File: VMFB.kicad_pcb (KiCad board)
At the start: 2 copper layers, 141.6 x 109.9 mm, 109 parts, among them J1 Barrel_Jack_Switch, J10 Conn_01x03_Pin, J11 Conn_01x08_Pin, J12 Conn_01x04_Pin, J13 Conn_01x04_Pin, J14 Conn_01x04_Pin, J2 USB_B, J3 Screw_Terminal_01x02, J4 Screw_Terminal_01x03, J5 Conn_01x03_Pin, J6 Conn_01x04_Pin, J7 Conn_01x04_Pin, J8 Conn_01x04_Pin, J9 Conn_01x02_Pin, Q1 BC547, Q2 BC547, Q3 BC547, Q4 BD139, Q5 TIP41C, Q6 BC547, U1 LM358, U2 NE555P, U3 NE555P, U4 NE555P, U5 NE555P

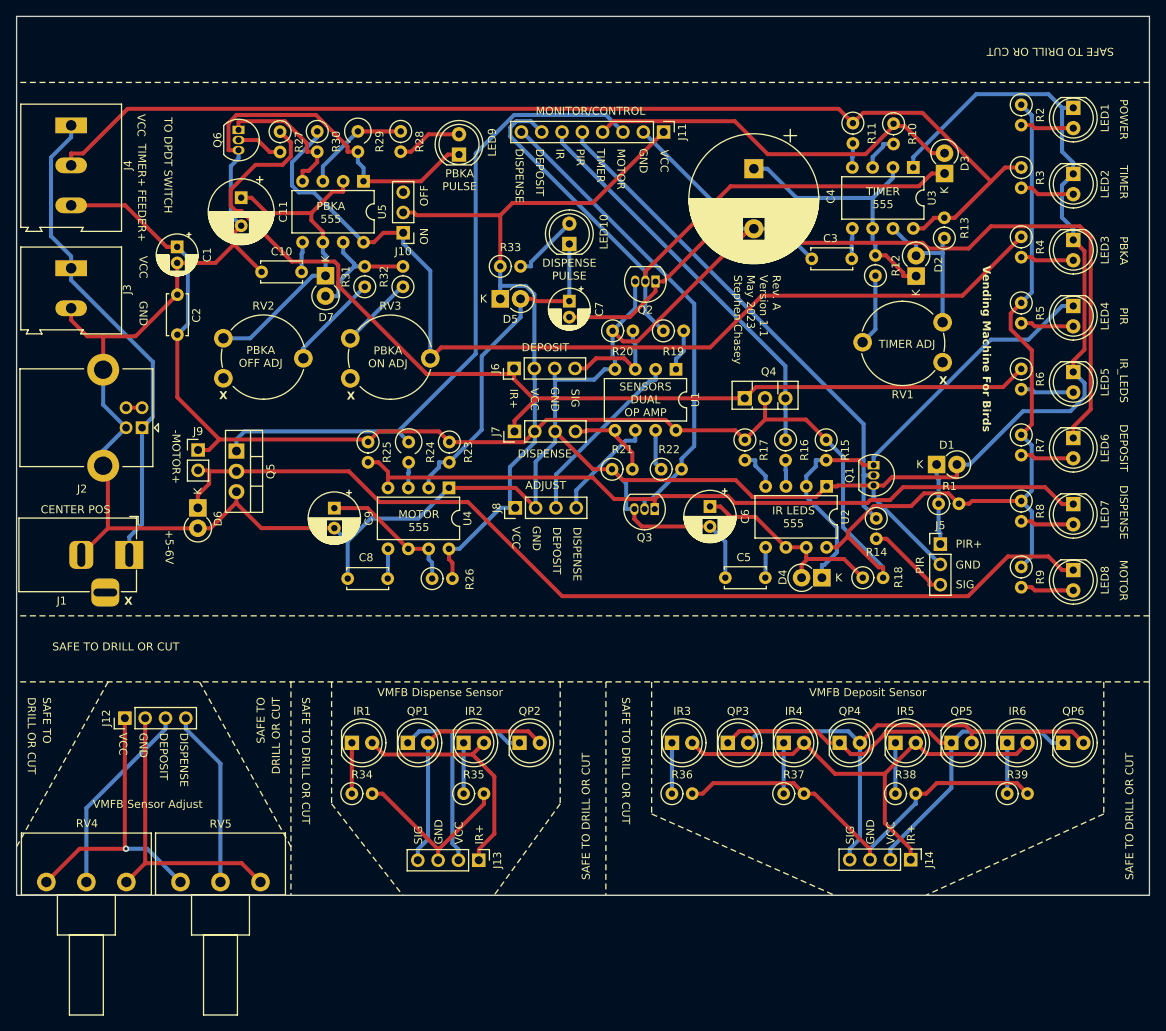
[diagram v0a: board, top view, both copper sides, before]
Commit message: Added 1uf cap on the dispense transistor base to prevent triggering on power-up.
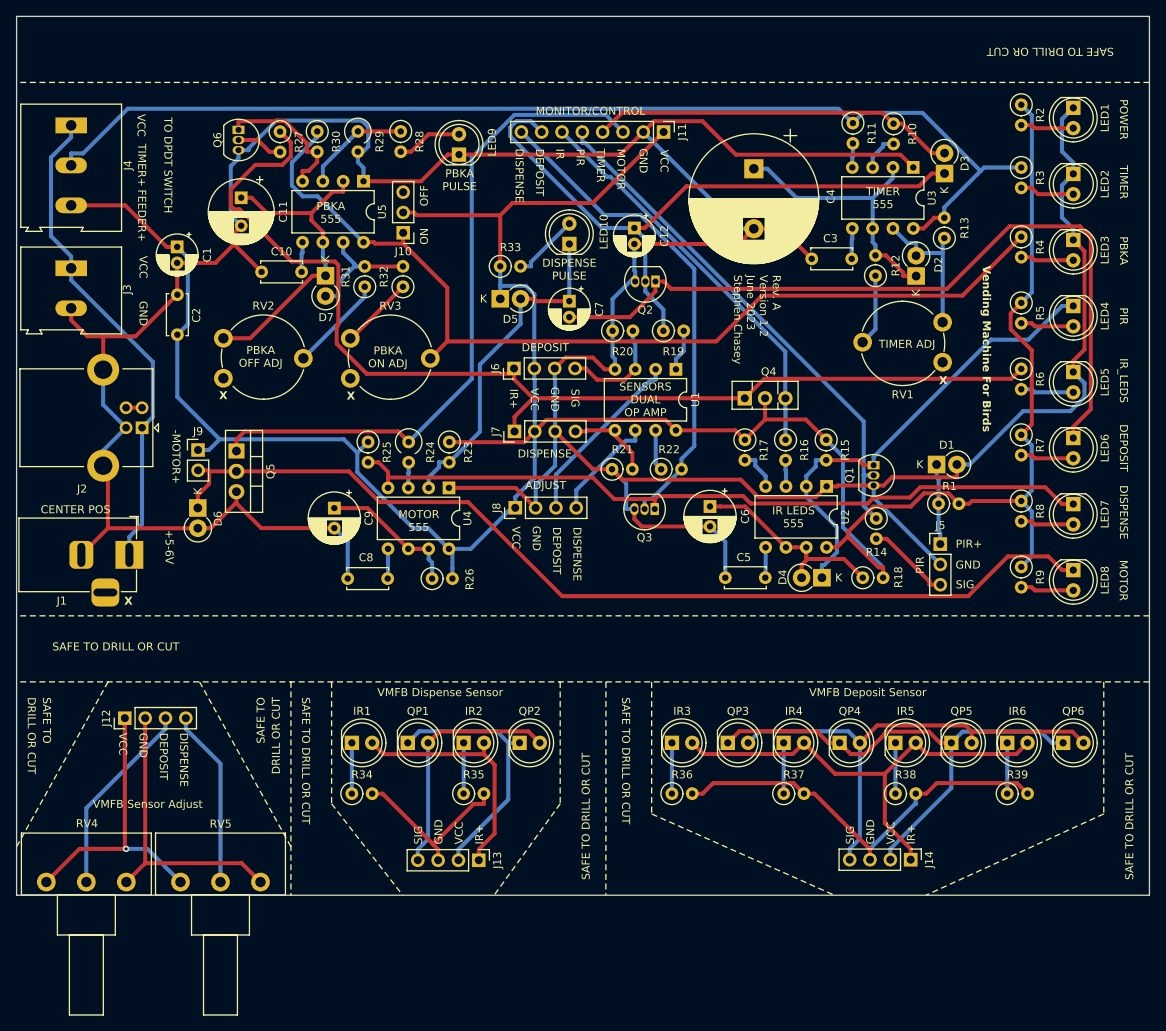
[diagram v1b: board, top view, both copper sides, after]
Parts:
- added C12: 1uF, Capacitor_THT:CP_Radial_D5.0mm_P2.00mm, F.Cu at (148.3, 58.2)
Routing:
- net GND: track 454.5 -> 473.4 mm
- net VCC: track 342.8 -> 350.8 mm
- net IR+: track 132.9 -> 137.5 mm
- net DISPENSE MON: track 59.1 -> 61.8 mm
- net Net-(LED6-K): track 100.6 -> 98.0 mm
- net TIMER MON: track 47.9 -> 45.8 mm
- net Net-(J10-Pin_1): track 122.6 -> 121.0 mm
- net TIMER+: track 140.3 -> 139.2 mm
- net Net-(J13-Pin_2): track 31.6 -> 32.4 mm
- net MOTOR MON: track 84.0 -> 84.8 mm
- net Net-(D2-A): track 18.5 -> 19.2 mm
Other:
- board text added: "Rev. A Version 1.2 June 2023 Stephen Chasey"
- board text removed: "Rev. A Version 1.1 May 2023 Stephen Chasey"

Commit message: Swapped PIR+ and GND to better accomodate common PIR pinouts.
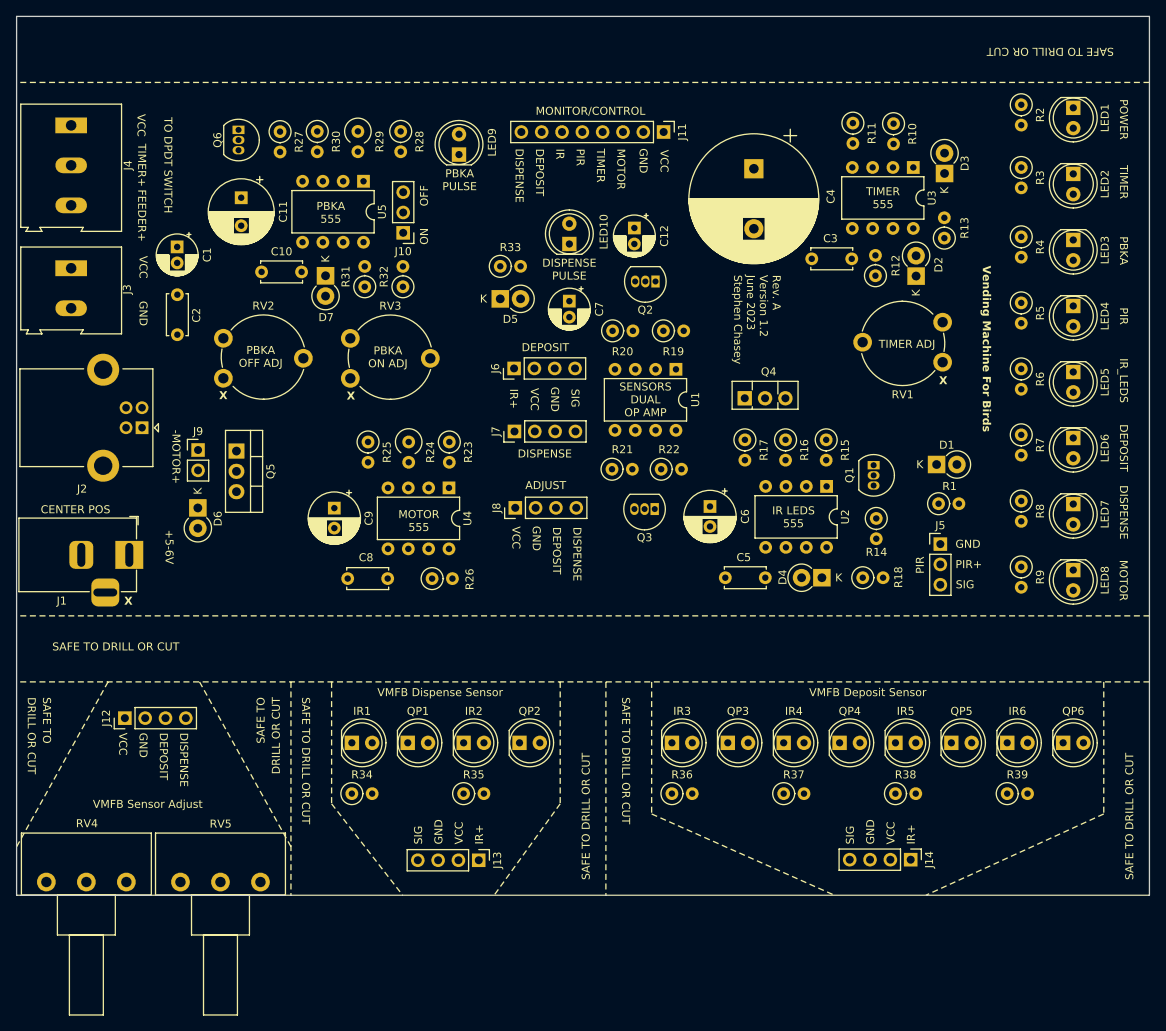
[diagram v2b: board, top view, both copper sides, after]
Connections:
- J5 pad 1: PIR+ -> GND
- J5 pad 2: GND -> PIR+
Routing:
- net GND: track 473.4 -> 0.00 mm
- net VCC: track 350.8 -> 0.00 mm
- net TIMER+: track 139.2 -> 0.00 mm
- net IR+: track 137.5 -> 0.00 mm
- net Net-(D6-K): track 123.9 -> 0.00 mm
- net Net-(J10-Pin_1): track 121.0 -> 0.00 mm
- net Net-(LED6-K): track 98.0 -> 0.00 mm
- net MOTOR RESET: track 95.3 -> 0.00 mm
- net MOTOR MON: track 84.8 -> 0.00 mm
- net DEPOSIT MON: track 82.1 -> 0.00 mm
- net PIR MON: track 65.0 -> 0.00 mm
- net Net-(J14-Pin_2): track 64.4 -> 0.00 mm
- net DISPENSE MON: track 61.8 -> 0.00 mm
- net Net-(J14-Pin_4): track 61.5 -> 0.00 mm
- net Net-(J2-VBUS): track 61.2 -> 0.00 mm
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
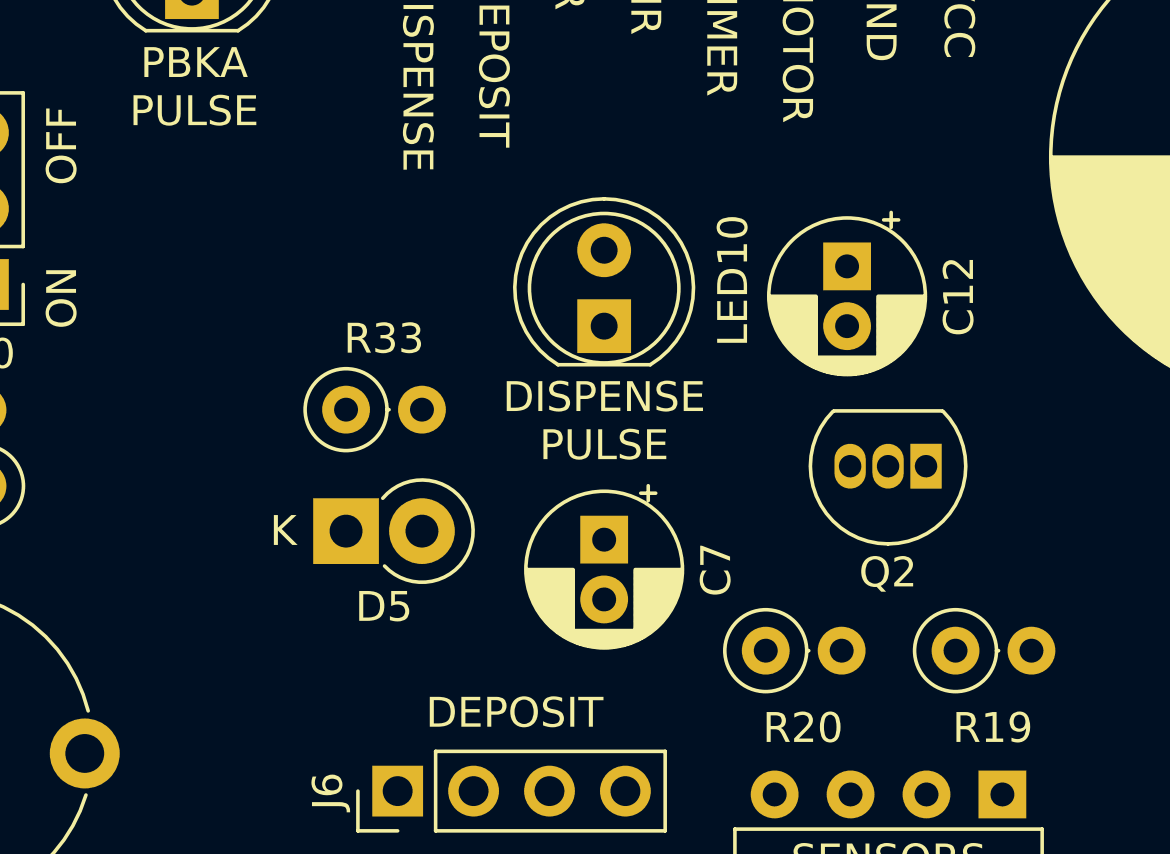
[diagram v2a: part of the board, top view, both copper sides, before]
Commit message: Added 100K bleeder resistor across the pulse-shortening cap C7
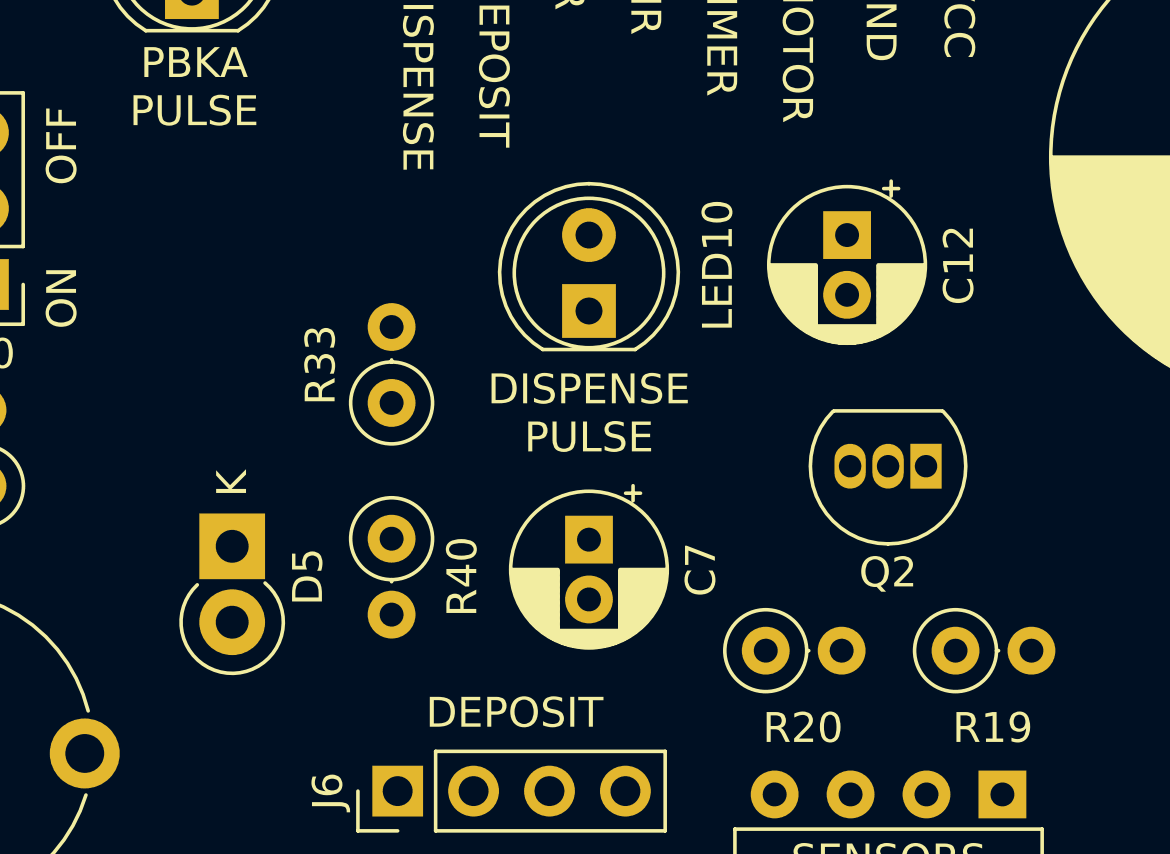
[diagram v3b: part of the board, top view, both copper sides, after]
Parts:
- added R40: 100K, Resistor_THT:R_Axial_DIN0207_L6.3mm_D2.5mm_P2.54mm_Vertical, F.Cu at (133.1, 67.3)
- moved D5 3.84 mm to (127.8, 67.6), turned to -90 degrees
- moved R33 1.54 mm to (133.1, 62.8), turned to 90 degrees
- moved C12 1.05 mm to (148.3, 57.1)
- moved LED10 0.72 mm to (139.7, 59.7)
- moved C7 0.51 mm to (139.7, 67.3)

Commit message: changed external header to 6-pin with pinout to match most 4-channel level shifters, removed 2 unnecessary 10K reset resistors from timer and IR power 555s
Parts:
- removed R11, R17: 10K, Resistor_THT:R_Axial_DIN0207_L6.3mm_D2.5mm_P2.54mm_Vertical
- J11: value Conn_01x08_Pin -> Conn_01x06_Pin; footprint Connector_PinHeader_2.54mm:PinHeader_1x08_P2.54mm_Vertical -> Connector_PinHeader_2.54mm:PinHeader_1x06_P2.54mm_Vertical
- moved J11 15.3 mm to (136.7, 46.2), turned to 90 degrees
- moved D3 14.9 mm to (172.7, 47.7)
- moved R10 2.68 mm to (178.1, 45.2)
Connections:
- D3 pad 2: TIMER MON -> Net-(D3-A)
- J11 pad 1: VCC -> GND
- J11 pad 2: GND -> DISPENSE MON
- J11 pad 3: MOTOR MON -> DEPOSIT MON
- J11 pad 4: TIMER MON -> IR MON
- J11 pad 6: IR MON -> VCC
- Q5 pad 1: MOTOR MON -> Net-(Q5-B)
- R10 pad 1: TIMER MON -> Net-(D3-A)
- R24 pad 1: MOTOR MON -> Net-(Q5-B)
- U2 pad 4: Net-(U2-R) -> VCC
- U3 pad 4: Net-(U3-R) -> TIMER+
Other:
- board text added: "DEP"
- board text added: "DIS"

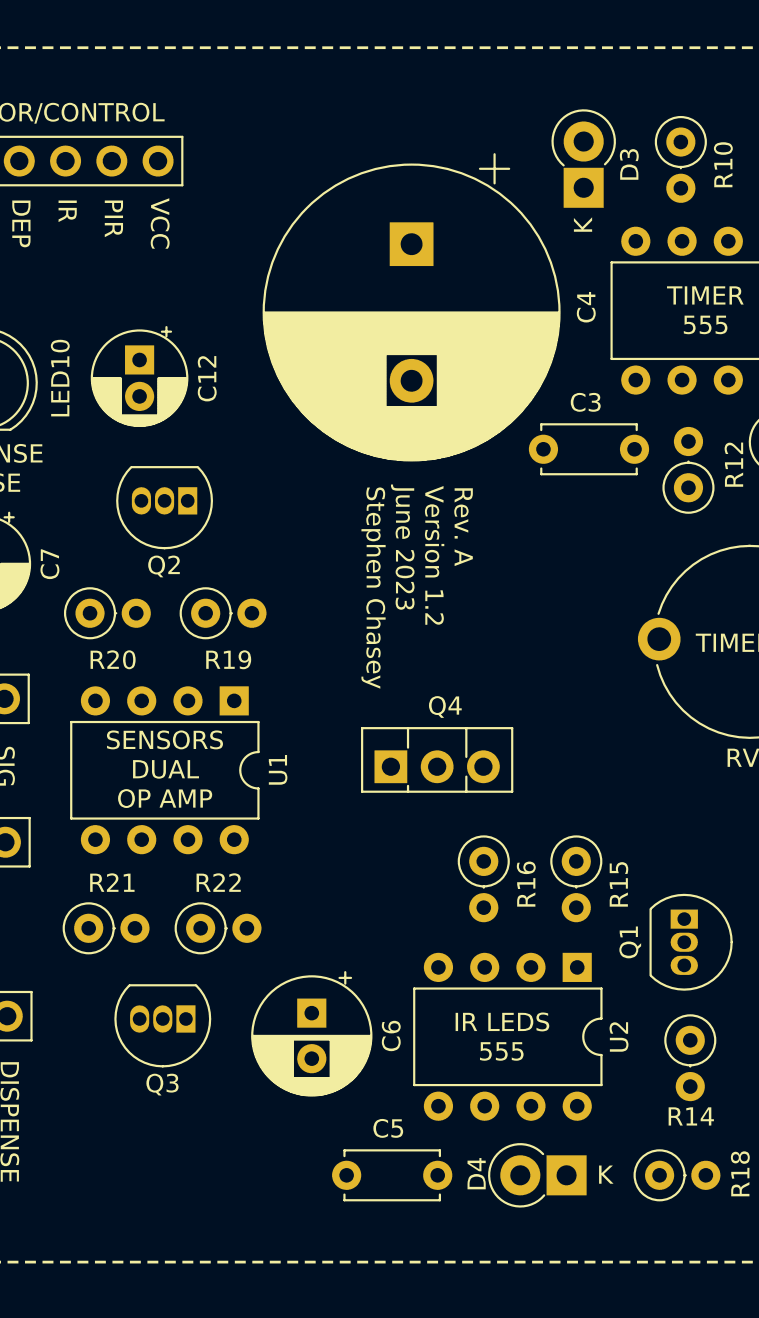
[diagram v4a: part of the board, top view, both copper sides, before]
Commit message: added another 1uf cap across the dispense sensor so like the dispense sensor it won't trigger on power up.
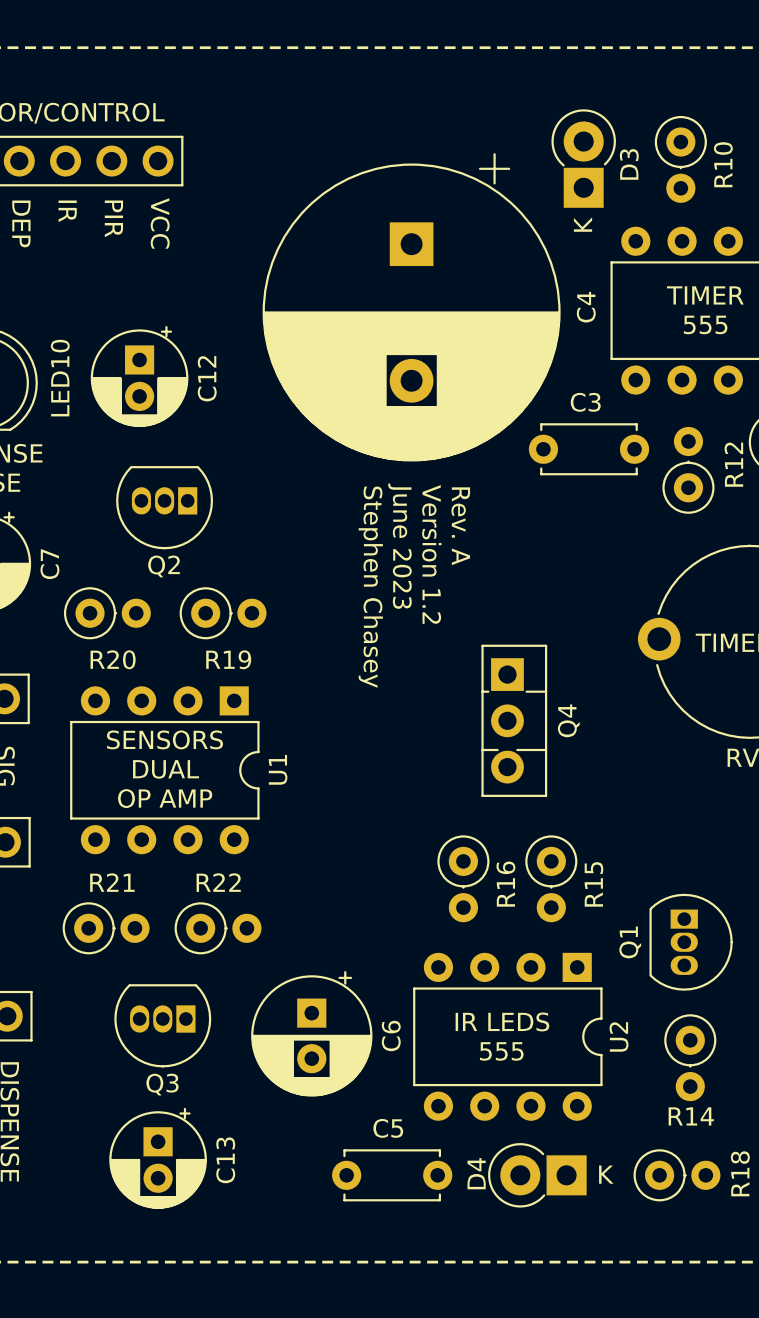
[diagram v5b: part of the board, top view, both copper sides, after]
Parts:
- added C13: 1uF, Capacitor_THT:CP_Radial_D5.0mm_P2.00mm, F.Cu at (149.4, 100.1)
- moved Q4 8.16 mm to (168.5, 74.4), turned to -90 degrees
- moved R15 1.37 mm to (170.9, 84.7)
- moved R16 1.12 mm to (166.1, 84.7)
